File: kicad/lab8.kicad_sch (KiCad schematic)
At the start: 52 parts, among them Q1 LTR3208E, SW1 Reset, U3 MCP6294, U4 PIC32MX170F256B, U5 LM339AN

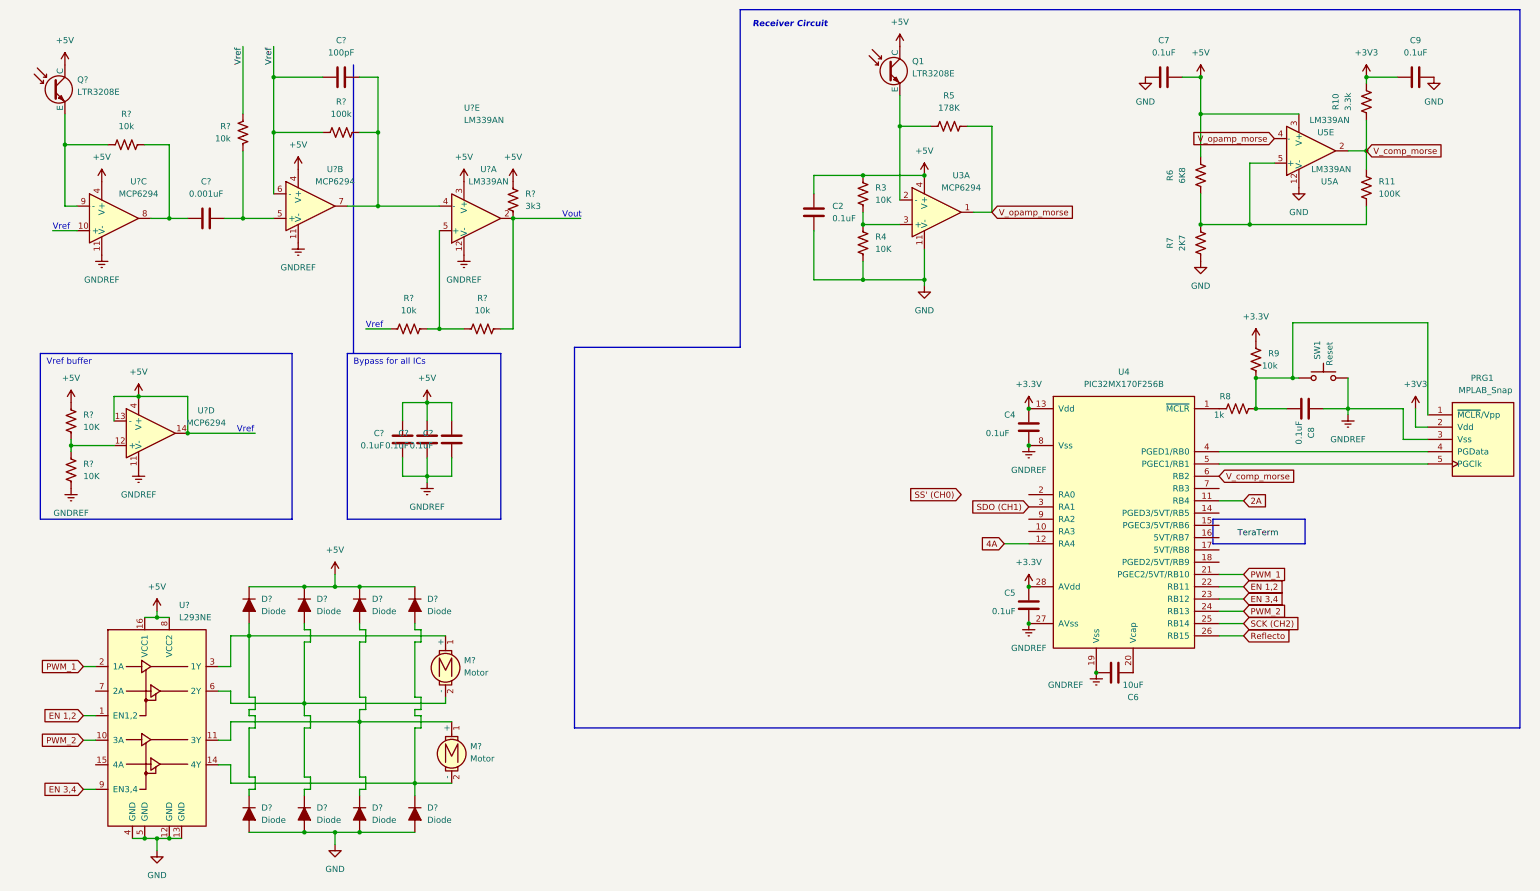
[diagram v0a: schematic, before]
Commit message: Finalize IR receiver schematic
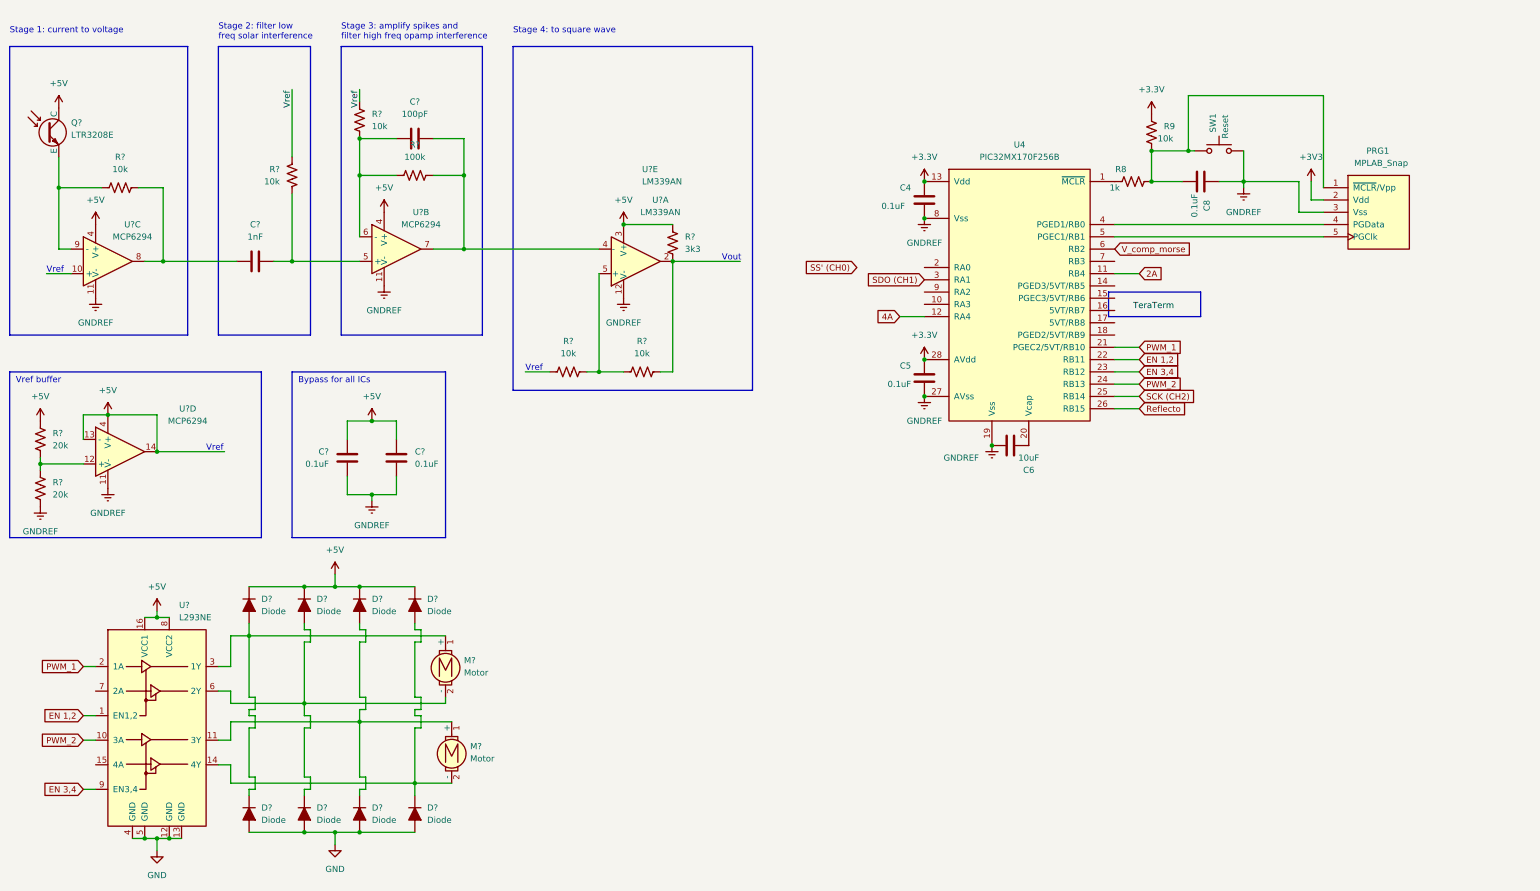
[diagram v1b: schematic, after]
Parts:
- removed C2, C7, C9, C? (x3): 0.1uF, symbol ME218_BaseLib:Cap
- removed C?: 100pF, symbol ME218_BaseLib:Cap
- removed C?: 0.001uF, symbol ME218_BaseLib:Cap
- removed Q1, Q?: LTR3208E, symbol ME218_BaseLib:Photo_NPN
- removed R10: 3.3k, symbol ME218_BaseLib:Res1
- removed R11: 100K, symbol ME218_BaseLib:Res1
- removed R3, R4, R? (x2): 10K, symbol ME218_BaseLib:Res1
- removed R5: 178K, symbol ME218_BaseLib:Res1
- removed R6: 6K8, symbol ME218_BaseLib:Res1
- removed R7: 2K7, symbol ME218_BaseLib:Res1
- removed R? (x4): 10k, symbol ME218_BaseLib:Res1
- removed R?: 100k, symbol ME218_BaseLib:Res1
- removed R?: 3k3, symbol ME218_BaseLib:Res1
- removed U3, U? (x3): MCP6294, symbol ME218_BaseLib:MCP6294
- removed U5, U? (x2): LM339AN, symbol ME218_BaseLib:LM339AN
- added C? (x2): 0.1uF, symbol ME218_BaseLib:Cap
- added C?: 100pF, symbol ME218_BaseLib:Cap
- added C?: 1nF, symbol ME218_BaseLib:Cap
- added Q?: LTR3208E, symbol ME218_BaseLib:Photo_NPN
- added R?: 100k, symbol ME218_BaseLib:Res1
- added R? (x2): 20k, symbol ME218_BaseLib:Res1
- added R? (x5): 10k, symbol ME218_BaseLib:Res1
- added R?: 3k3, symbol ME218_BaseLib:Res1
- added U? (x2): LM339AN, symbol ME218_BaseLib:LM339AN
- added U? (x3): MCP6294, symbol ME218_BaseLib:MCP6294
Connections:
- net +5V: now also C?.1, C?.1, Q?.1 (C), R?.1, R?.1, U?.13 (-), U?.14, U?.3 (V+), U?.4 (V+), U?.4 (V+), U?.4 (V+)
- net GNDREF: now also C?.2, C?.2, R?.2, U?.11 (V-), U?.11 (V-), U?.11 (V-), U?.12 (V-)
- net Vref: now also R?.2
- new net: C?.1, R?.1, R?.1, U?.6 (-)
- new net: C?.2, R?.2, U?.4 (-), U?.7
- new net: R?.1, R?.2, U?.12 (+)
- new net: C?.2, R?.1, U?.5 (+)
- new net: Q?.2 (E), R?.1, U?.9 (-)
- new net: C?.1, R?.2, U?.8
- new net: R?.1, R?.2, U?.5 (+)
- new net: R?.2, R?.2, U?.2
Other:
- note added: "Stage 1: current to voltage"
- note added: "Stage 2: filter low freq solar interference"
- note added: "Stage 3: amplify spikes and filter high freq opamp interference"
- note added: "Stage 4: to square wave"
- note removed: "Receiver Circuit"
- moved on the sheet: C4, C5, C6, C8, PRG1, R8, R9, SW1, U4

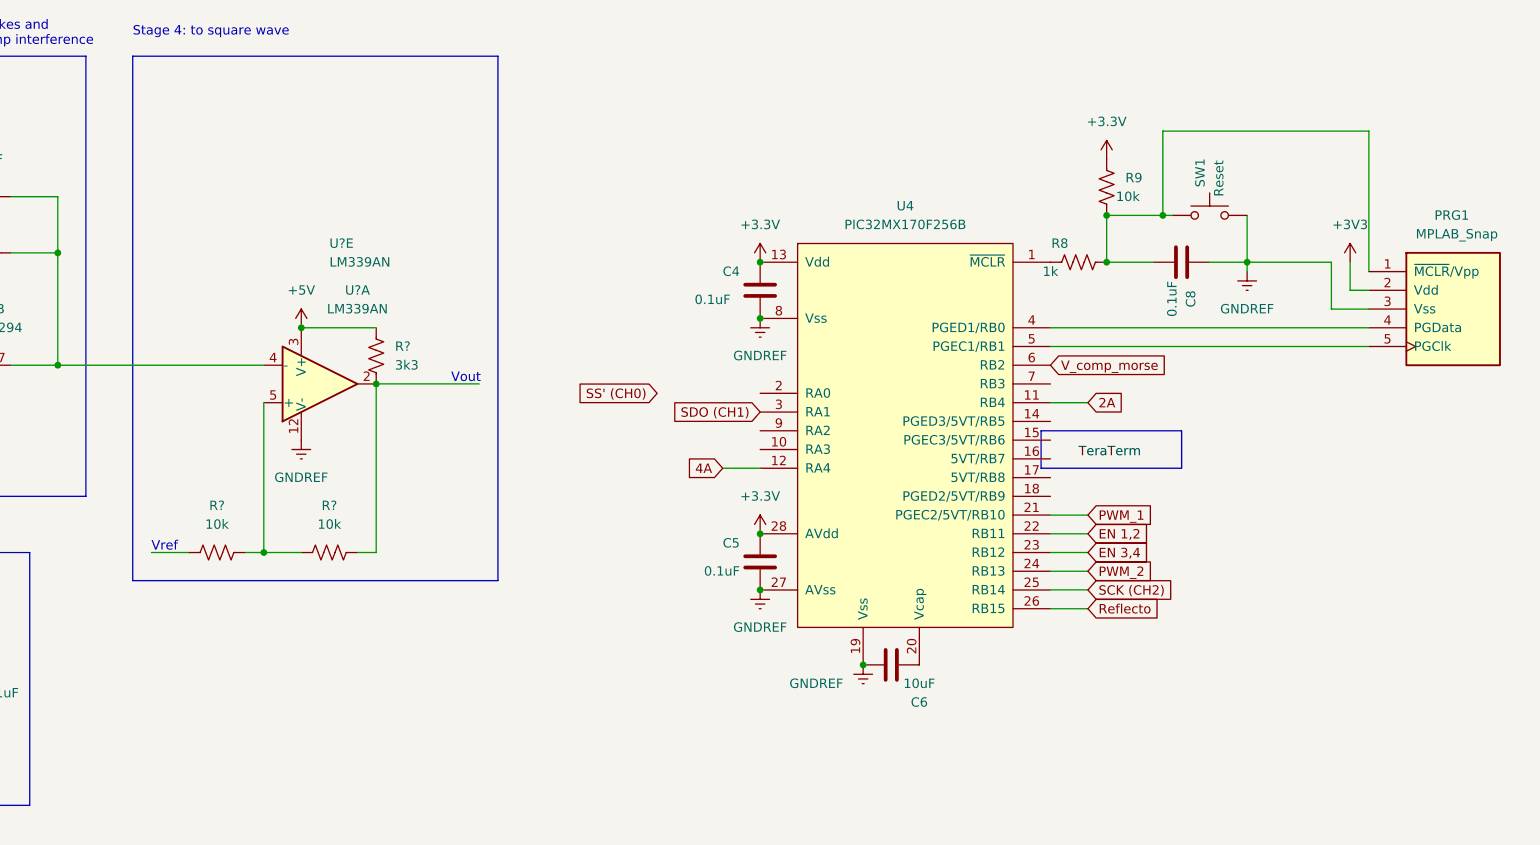
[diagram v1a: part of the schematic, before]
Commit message: include SPI lines in kicad.
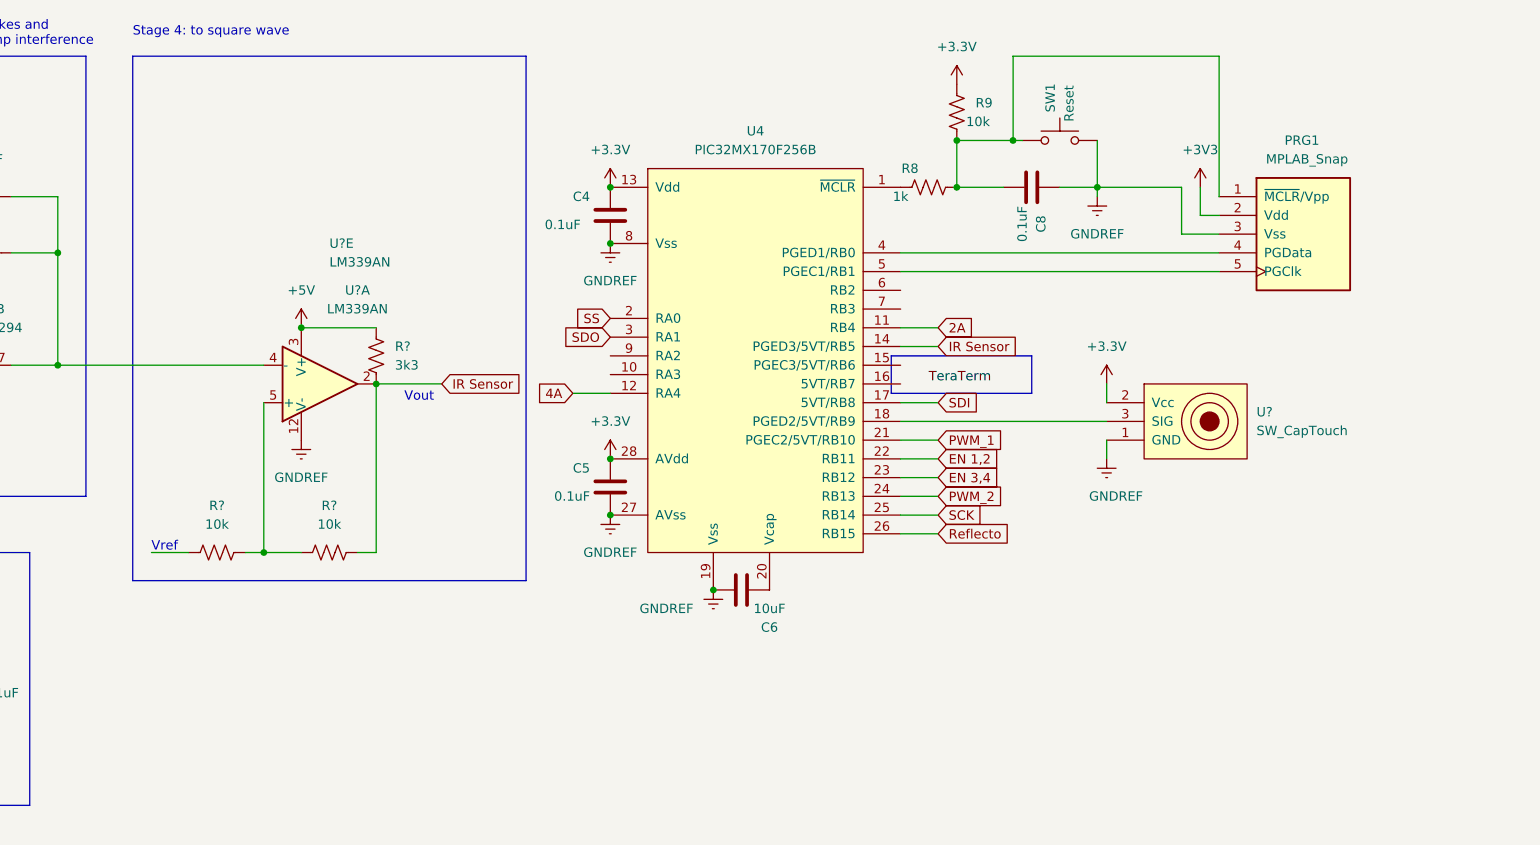
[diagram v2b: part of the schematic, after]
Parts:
- added U?: SW_CapTouch, symbol 218 spdl:SW_CapTouch
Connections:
- net +3.3V: now also U?.2 (Vcc)
- net GNDREF: now also U?.1 (GND)
- net IR Sensor: now reaches U4.14 (PGED3/5VT/RB5)
- net IR Sensor: now also R?.2, R?.2, U?.2
- net SDI: now reaches U4.17 (5VT/RB8)
- net at U4.18 (PGED2/5VT/RB9): now also U?.3 (SIG)
- net SS: now reaches U4.2 (RA0)
- net SCK (CH2) renamed SCK
- net SDO (CH1) renamed SDO
- net V_comp_morse: no longer names the net of U4.6 (RB2)
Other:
- moved on the sheet: C4, C5, C6, C8, PRG1, R8, R9, SW1, U4

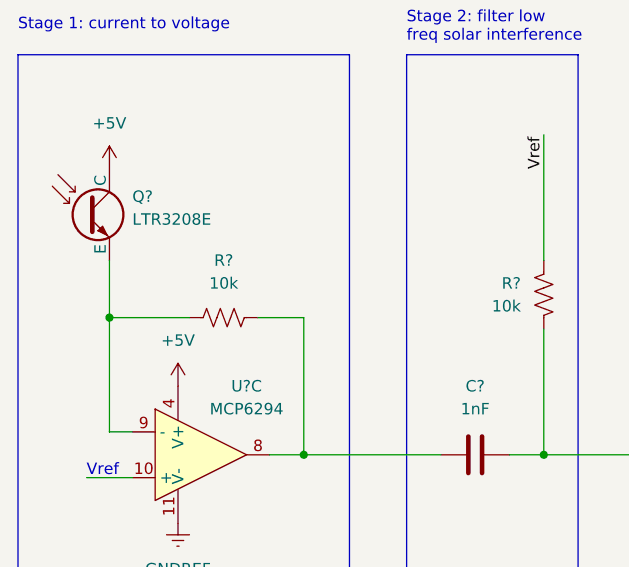
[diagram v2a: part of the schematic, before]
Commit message: Increase gain in first stage opamp
* Can now detect beacon from end of field, originally could only 2/3 way
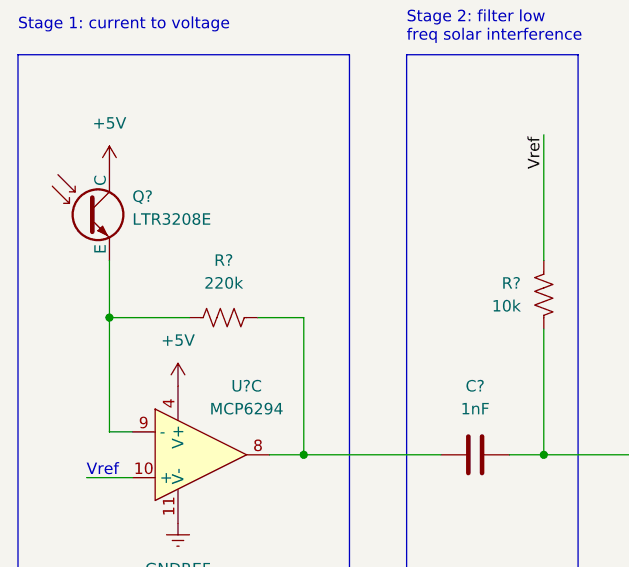
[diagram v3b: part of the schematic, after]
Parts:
- R?: value 10k -> 220k
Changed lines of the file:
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@@
     (in_bom yes) (on_board yes) (fields_autoplaced)
     (property "Reference" "R?" (id 0) (at 38.1 41.91 90))
-    (property "Value" "10k" (id 1) (at 38.1 44.45 90))
+    (property "Value" "220k" (id 1) (at 38.1 44.45 90))
     (property "Footprint" "" (id 2) (at 38.354 47.244 90)
       (effects (font (size 1.27 1.27)) hide)
@@
     )
     (path "/629c942a-6f8e-4978-852f-a7c494bd2d52"
-      (reference "R?") (unit 1) (value "10k") (footprint "")
+      (reference "R?") (unit 1) (value "220k") (footprint "")
     )
     (path "/769a2a22-c34d-4b0c-85d2-778f408fab52"
